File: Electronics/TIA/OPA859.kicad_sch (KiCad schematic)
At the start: 13 parts, among them U4 ${SIM.PARAMS}

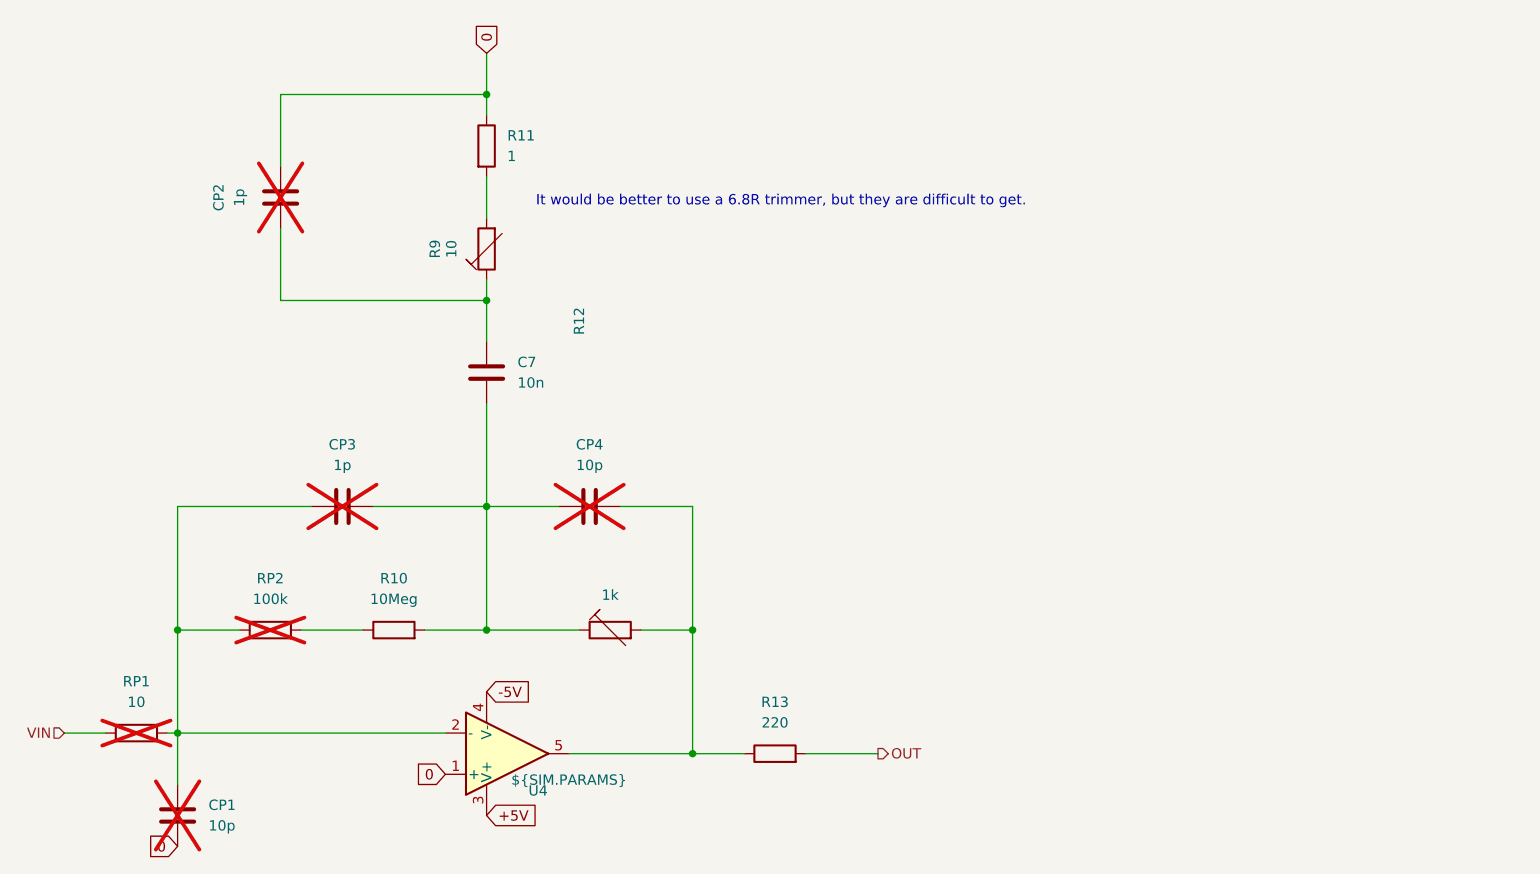
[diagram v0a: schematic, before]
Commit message: Make the simulation circuit tidier
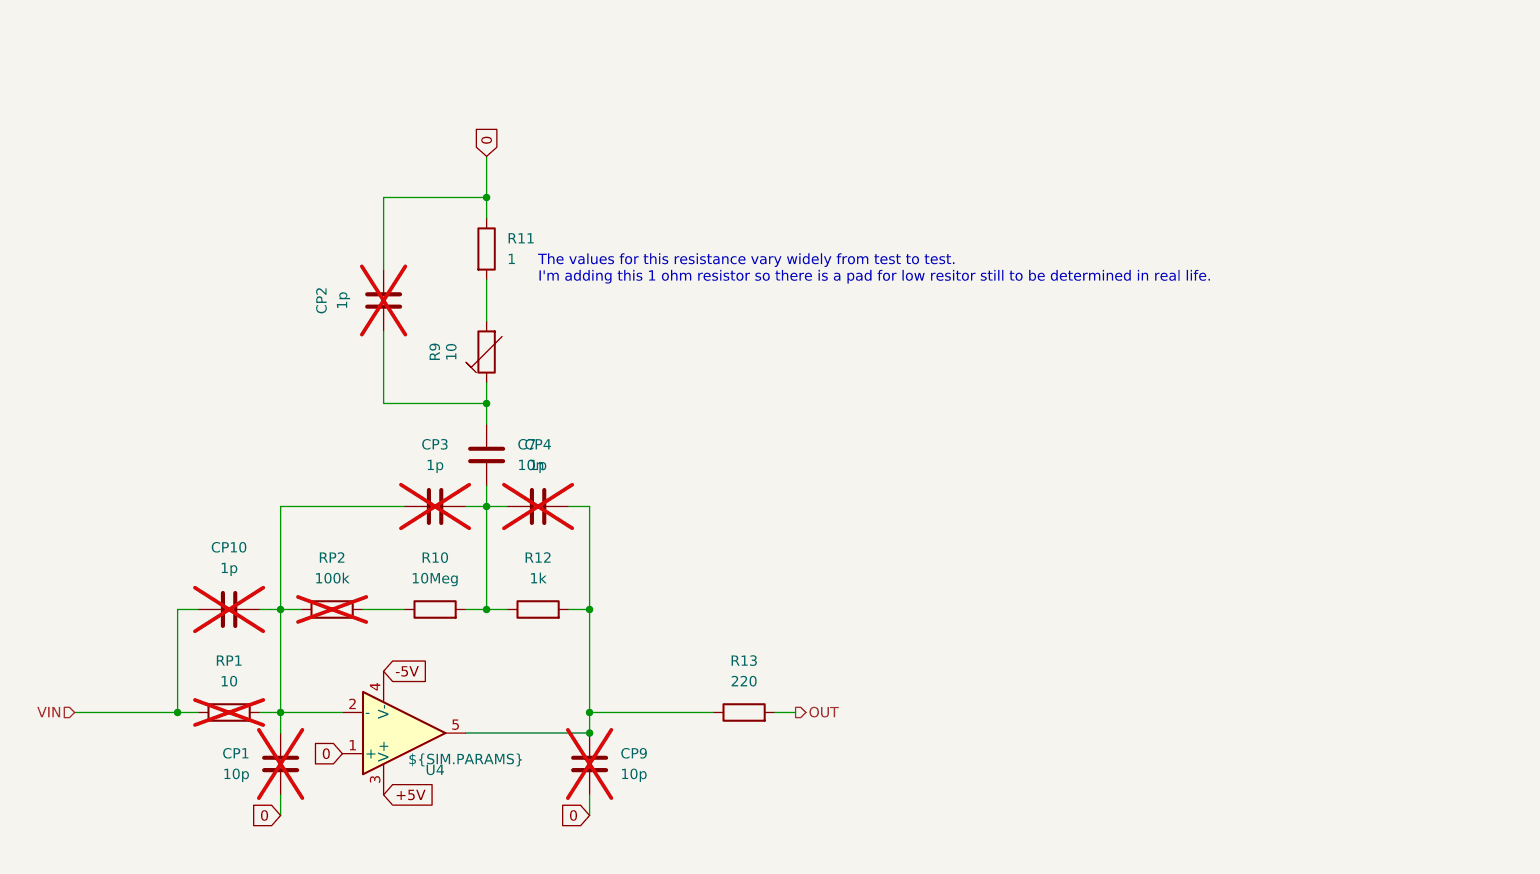
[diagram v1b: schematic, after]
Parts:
- removed R12: 1k, symbol Device:R_Trim
- added CP10: 1p, symbol Device:C
- added CP9: 10p, symbol Device:C
- added R12: 1k, symbol Device:R
- CP4: value 10p -> 1p
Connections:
- net 0: now also CP9.1
- net VIN: now also CP10.1
- net at CP1.1, CP3.1, RP1.2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: now also CP10.2
- net at C7.2, CP3.2, CP4.1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: now also R12.1
- net at CP4.2, R13.1, U4.5: now also CP9.2, R12.2
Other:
- note added: "The values for this resistance vary widely from test to test. I'm adding this 1 ohm resistor so there is a pad for low resitor still to be determined in real life."
- note removed: "It would be better to use a 6.8R trimmer, but they are difficult to get."
- moved on the sheet: C7, CP1, CP2, CP3, CP4, R10, R11, R13, R9, RP1, RP2, U4
